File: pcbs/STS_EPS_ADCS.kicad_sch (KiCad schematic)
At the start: 25 parts, among them U10 MAX11632EEGT, U5 MAX11632EEGT, U6 MAX11632EEGT, U7 MAX11632EEGT, U8 MAX11632EEGT, U9 MAX11632EEGT

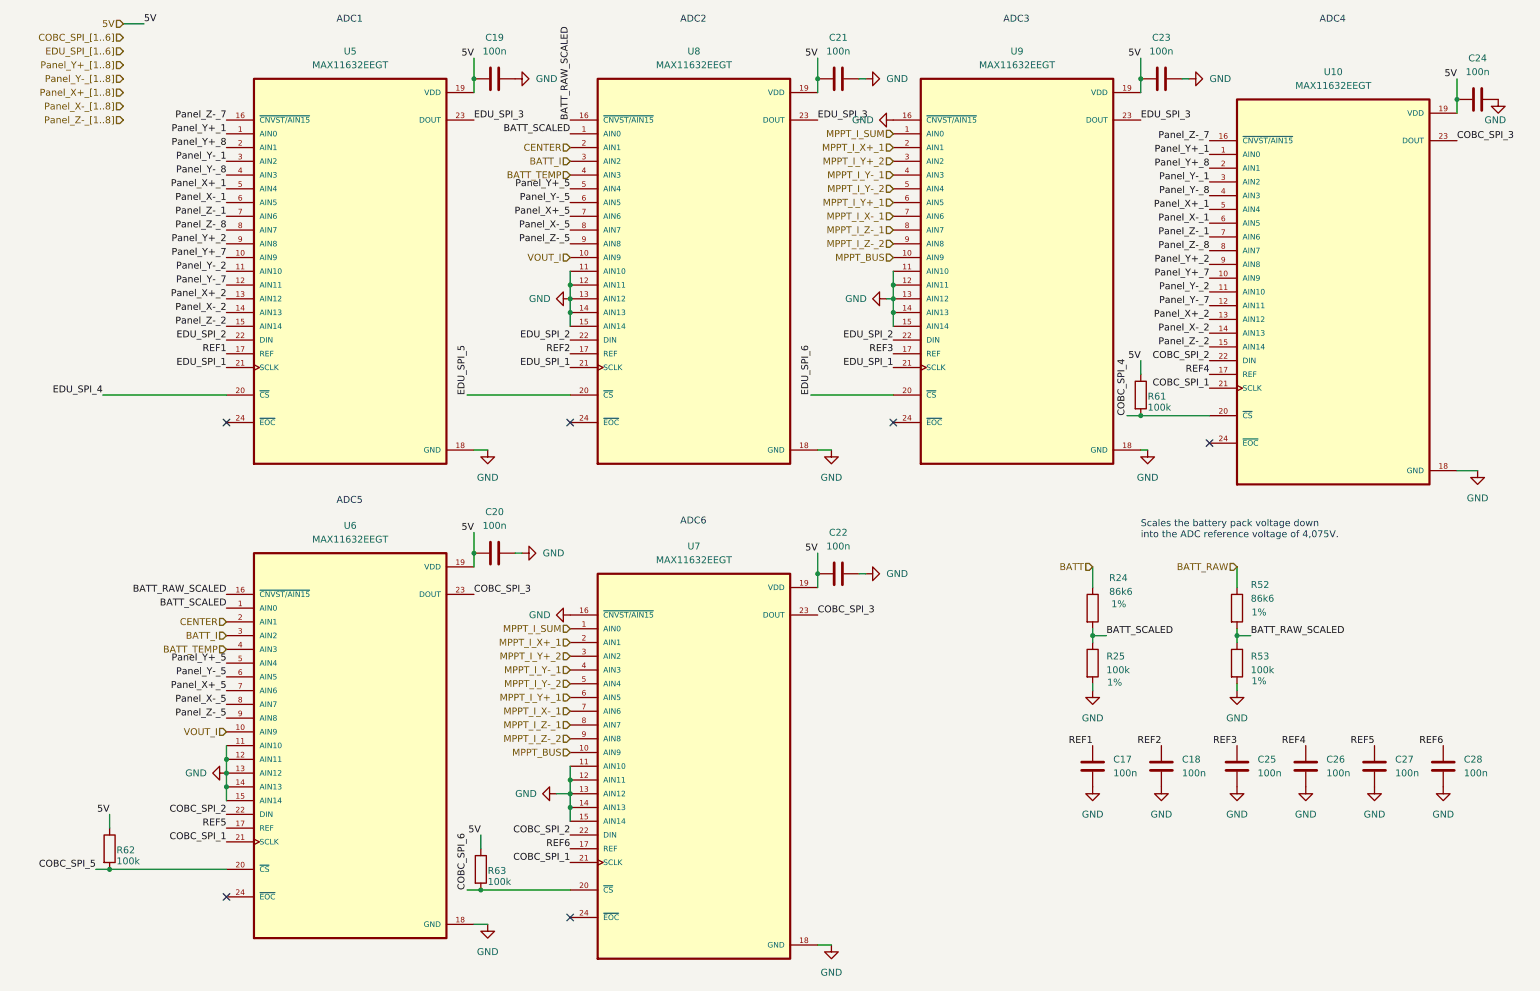
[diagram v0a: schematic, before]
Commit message: Changed net labels of the panel connectors, so they are consistent with the name of the respective connector.
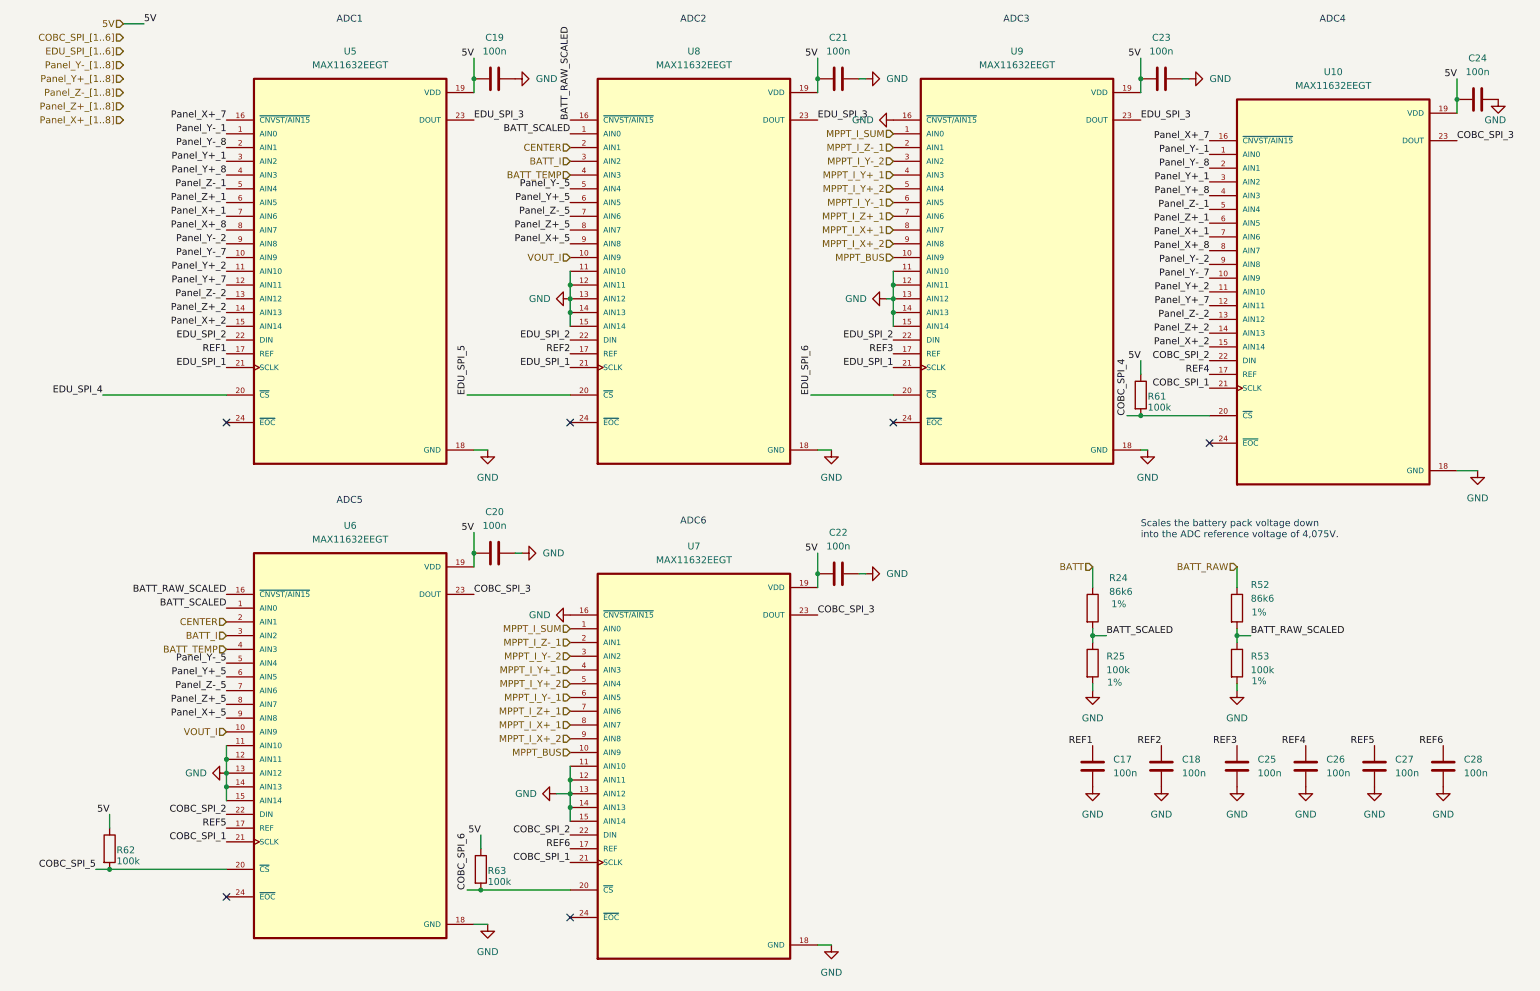
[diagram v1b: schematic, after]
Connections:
- net MPPT_I_X+_1: now also U7.8 (AIN7), U9.8 (AIN7); no longer U7.2 (AIN1), U9.2 (AIN1)
- net MPPT_I_Y+_1: now also U7.4 (AIN3), U9.4 (AIN3); no longer U7.6 (AIN5), U9.6 (AIN5)
- net MPPT_I_Y+_2: now also U7.5 (AIN4), U9.5 (AIN4); no longer U7.3 (AIN2), U9.3 (AIN2)
- net MPPT_I_Y-_1: now also U7.6 (AIN5), U9.6 (AIN5); no longer U7.4 (AIN3), U9.4 (AIN3)
- net MPPT_I_Y-_2: now also U7.3 (AIN2), U9.3 (AIN2); no longer U7.5 (AIN4), U9.5 (AIN4)
- net MPPT_I_Z-_1: now also U7.2 (AIN1), U9.2 (AIN1); no longer U7.8 (AIN7), U9.8 (AIN7)
- net Panel_X+_1: now also U10.7 (AIN6), U5.7 (AIN6); no longer U10.5 (AIN4), U5.5 (AIN4)
- net Panel_X+_2: now also U10.15 (AIN14), U5.15 (AIN14); no longer U10.13 (AIN12), U5.13 (AIN12)
- net Panel_X+_5: now also U6.9 (AIN8), U8.9 (AIN8); no longer U6.7 (AIN6), U8.7 (AIN6)
- net Panel_Y+_1: now also U10.3 (AIN2), U5.3 (AIN2); no longer U10.1 (AIN0), U5.1 (AIN0)
- net Panel_Y+_2: now also U10.11 (AIN10), U5.11 (AIN10); no longer U10.9 (AIN8), U5.9 (AIN8)
- net Panel_Y+_5: now also U6.6 (AIN5), U8.6 (AIN5); no longer U6.5 (AIN4), U8.5 (AIN4)
- net Panel_Y+_7: now also U10.12 (AIN11), U5.12 (AIN11); no longer U10.10 (AIN9), U5.10 (AIN9)
- net Panel_Y+_8: now also U10.4 (AIN3), U5.4 (AIN3); no longer U10.2 (AIN1), U5.2 (AIN1)
- net Panel_Y-_1: now also U10.1 (AIN0), U5.1 (AIN0); no longer U10.3 (AIN2), U5.3 (AIN2)
- net Panel_Y-_2: now also U10.9 (AIN8), U5.9 (AIN8); no longer U10.11 (AIN10), U5.11 (AIN10)
- net Panel_Y-_5: now also U6.5 (AIN4), U8.5 (AIN4); no longer U6.6 (AIN5), U8.6 (AIN5)
- net Panel_Y-_7: now also U10.10 (AIN9), U5.10 (AIN9); no longer U10.12 (AIN11), U5.12 (AIN11)
- net Panel_Y-_8: now also U10.2 (AIN1), U5.2 (AIN1); no longer U10.4 (AIN3), U5.4 (AIN3)
- net Panel_Z-_1: now also U10.5 (AIN4), U5.5 (AIN4); no longer U10.7 (AIN6), U5.7 (AIN6)
- net Panel_Z-_2: now also U10.13 (AIN12), U5.13 (AIN12); no longer U10.15 (AIN14), U5.15 (AIN14)
- net Panel_Z-_5: now also U6.7 (AIN6), U8.7 (AIN6); no longer U6.9 (AIN8), U8.9 (AIN8)
- net MPPT_I_X-_1 renamed MPPT_I_Z+_1
- net MPPT_I_Z-_2 renamed MPPT_I_X+_2
- net Panel_X-_1 renamed Panel_Z+_1
- net Panel_X-_2 renamed Panel_Z+_2
- net Panel_X-_5 renamed Panel_Z+_5
- net Panel_Z-_7 renamed Panel_X+_7
- net Panel_Z-_8 renamed Panel_X+_8

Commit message: Started adding part numbers to passive components.
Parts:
- C17, C18, C19, C20, C21, C22, C23, C24, C25, C26, C27, C28: Part Nr. (none) -> C0805T104K1RCLTU
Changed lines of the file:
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@@
 			)
 		)
+		(property "Part Nr." "C0805T104K1RCLTU"
+			(at 97.79 114.3 0)
+			(effects
+				(font
+					(size 1.27 1.27)
+				)
+				(hide yes)
+			)
+		)
 		(pin "1"
 		)
@@
 			)
 		)
+		(property "Part Nr." "C0805T104K1RCLTU"
+			(at 273.05 153.67 0)
+			(effects
+				(font
+					(size 1.27 1.27)
+				)
+				(hide yes)
+			)
+		)
 		(pin "1"
 		)
@@
 			)
 		)
+		(property "Part Nr." "C0805T104K1RCLTU"
+			(at 161.29 26.67 0)
+			(effects
+				(font
+					(size 1.27 1.27)
+				)
+				(hide yes)
+			)
+		)
 		(pin "1"
 		)
@@
 			)
 		)
+		(property "Part Nr." "C0805T104K1RCLTU"
+			(at 220.98 153.67 0)
+			(effects
+				(font
+					(size 1.27 1.27)
+				)
+				(hide yes)
+			)
+		)
 		(pin "1"
 		)
@@
 			)
 		)
+		(property "Part Nr." "C0805T104K1RCLTU"
+			(at 279.4 30.48 0)
+			(effects
+				(font
+					(size 1.27 1.27)
+				)
+				(hide yes)
+			)
+		)
 		(pin "1"
 		)
@@
 			)
 		)
+		(property "Part Nr." "C0805T104K1RCLTU"
+			(at 97.79 26.67 0)
+			(effects
+				(font
+					(size 1.27 1.27)
+				)
+				(hide yes)
+			)
+		)
 		(pin "1"
 		)
@@
 			)
 		)
+		(property "Part Nr." "C0805T104K1RCLTU"
+			(at 208.28 153.67 0)
+			(effects
+				(font
+					(size 1.27 1.27)
+				)
+				(hide yes)
+			)
+		)
 		(pin "1"
 		)
@@
 			)
 		)
+		(property "Part Nr." "C0805T104K1RCLTU"
+			(at 161.29 118.11 0)
+			(effects
+				(font
+					(size 1.27 1.27)
+				)
+				(hide yes)
+			)
+		)
 		(pin "1"
 		)
@@
 			)
 		)
+		(property "Part Nr." "C0805T104K1RCLTU"
+			(at 260.35 153.67 0)
+			(effects
+				(font
+					(size 1.27 1.27)
+				)
+				(hide yes)
+			)
+		)
 		(pin "1"
 		)
@@
 			)
 		)
+		(property "Part Nr." "C0805T104K1RCLTU"
+			(at 234.95 153.67 0)
+			(effects
+				(font
+					(size 1.27 1.27)
+				)
+				(hide yes)
+			)
+		)
 		(pin "1"
 		)
@@
 			)
 		)
+		(property "Part Nr." "C0805T104K1RCLTU"
+			(at 247.65 153.67 0)
+			(effects
+				(font
+					(size 1.27 1.27)
+				)
+				(hide yes)
+			)
+		)
 		(pin "1"
 		)
@@
 			(at 220.98 26.67 0)
 			(effects
+				(font
+					(size 1.27 1.27)
+				)
+				(hide yes)
+			)
+		)
+		(property "Part Nr." "C0805T104K1RCLTU"
+			(at 220.98 26.67 0)
+			(effects

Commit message: Added part numbers to components of STS1_EPS_1.
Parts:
- R24, R52: Part Nr. (none) -> RCA080586K6FKEA
- R25, R53, R61, R62, R63: Part Nr. (none) -> TNPW0805100KFEEA
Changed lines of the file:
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@@
+			)
+		)
+		(property "Part Nr." "RCA080586K6FKEA"
+			(at 208.28 124.46 0)
+			(effects
+				(font
+					(size 1.27 1.27)
+				)
+				(hide yes)
 			)
 		)
@@
 			)
 		)
+		(property "Part Nr." "TNPW0805100KFEEA"
+			(at 234.95 134.62 0)
+			(effects
+				(font
+					(size 1.27 1.27)
+				)
+				(hide yes)
+			)
+		)
 		(pin "1"
 		)
@@
 			)
 		)
+		(property "Part Nr." "TNPW0805100KFEEA"
+			(at 26.67 168.91 0)
+			(effects
+				(font
+					(size 1.27 1.27)
+				)
+				(hide yes)
+			)
+		)
 		(pin "1"
 		)
@@
 			)
 		)
+		(property "Part Nr." "TNPW0805100KFEEA"
+			(at 217.17 85.09 0)
+			(effects
+				(font
+					(size 1.27 1.27)
+				)
+				(hide yes)
+			)
+		)
 		(pin "1"
 		)
@@
 			)
 		)
+		(property "Part Nr." "TNPW0805100KFEEA"
+			(at 208.28 134.62 0)
+			(effects
+				(font
+					(size 1.27 1.27)
+				)
+				(hide yes)
+			)
+		)
 		(pin "1"
 		)
@@
 			)
 		)
+		(property "Part Nr." "TNPW0805100KFEEA"
+			(at 95.25 172.72 0)
+			(effects
+				(font
+					(size 1.27 1.27)
+				)
+				(hide yes)
+			)
+		)
 		(pin "1"
 		)
@@
 			)
 		)
+		(property "Part Nr." "RCA080586K6FKEA"
+			(at 234.95 124.46 0)
+			(effects
+				(font
+					(size 1.27 1.27)
+				)
+				(hide yes)
+			)
+		)

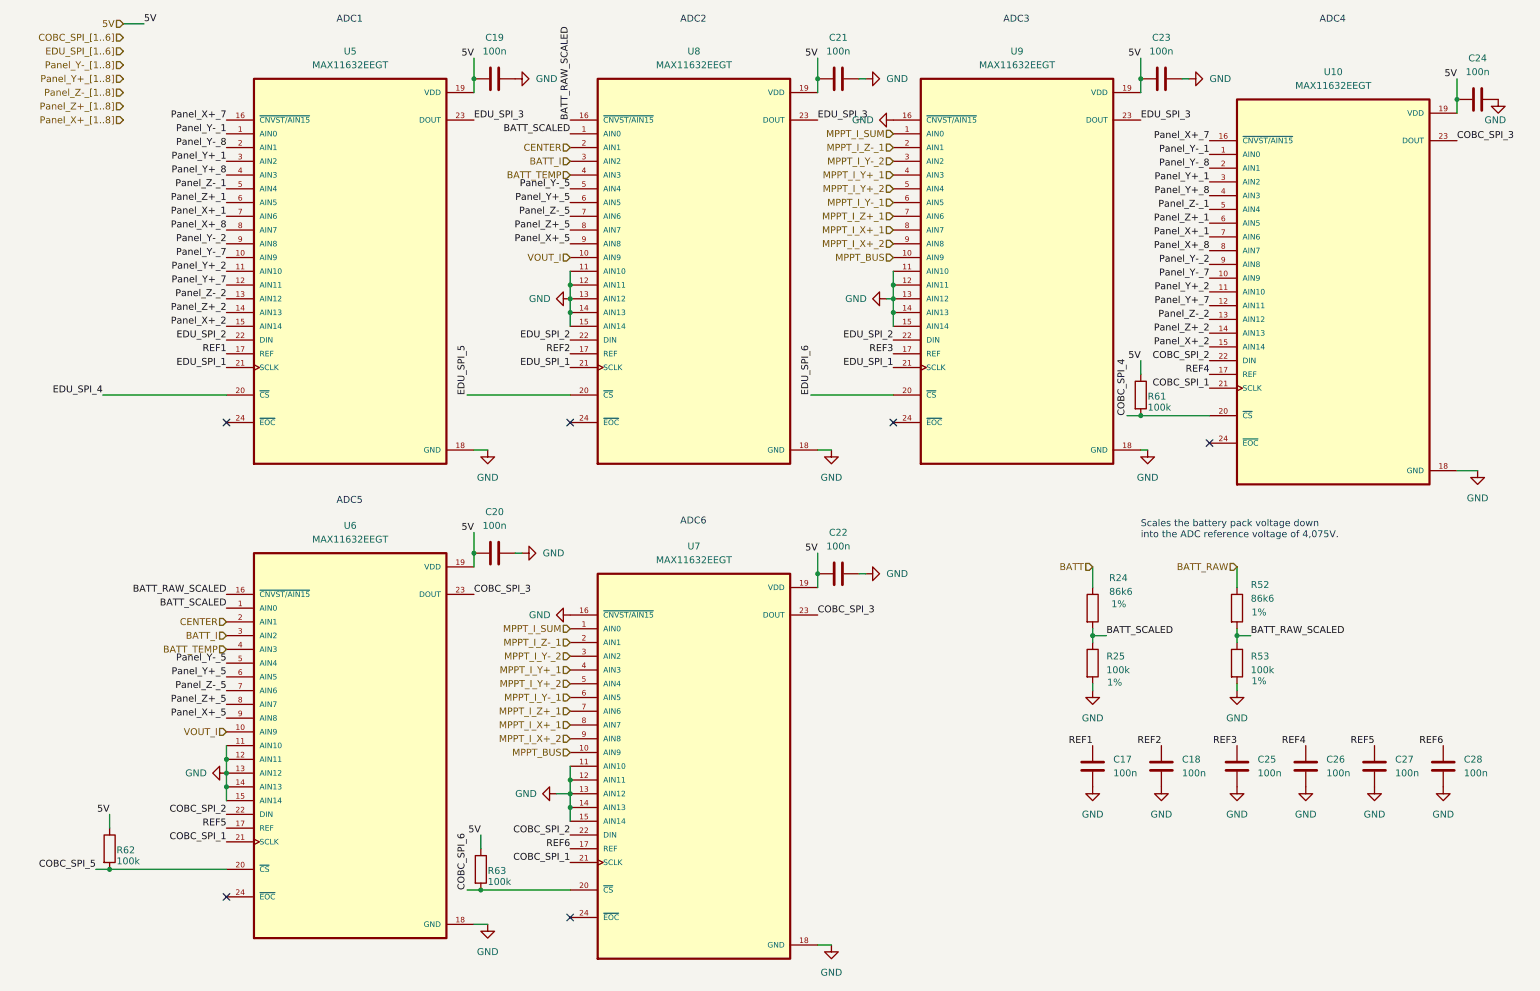
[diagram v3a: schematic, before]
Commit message: Added FETs to the CS pins of the EDU's housekeeping data interface.
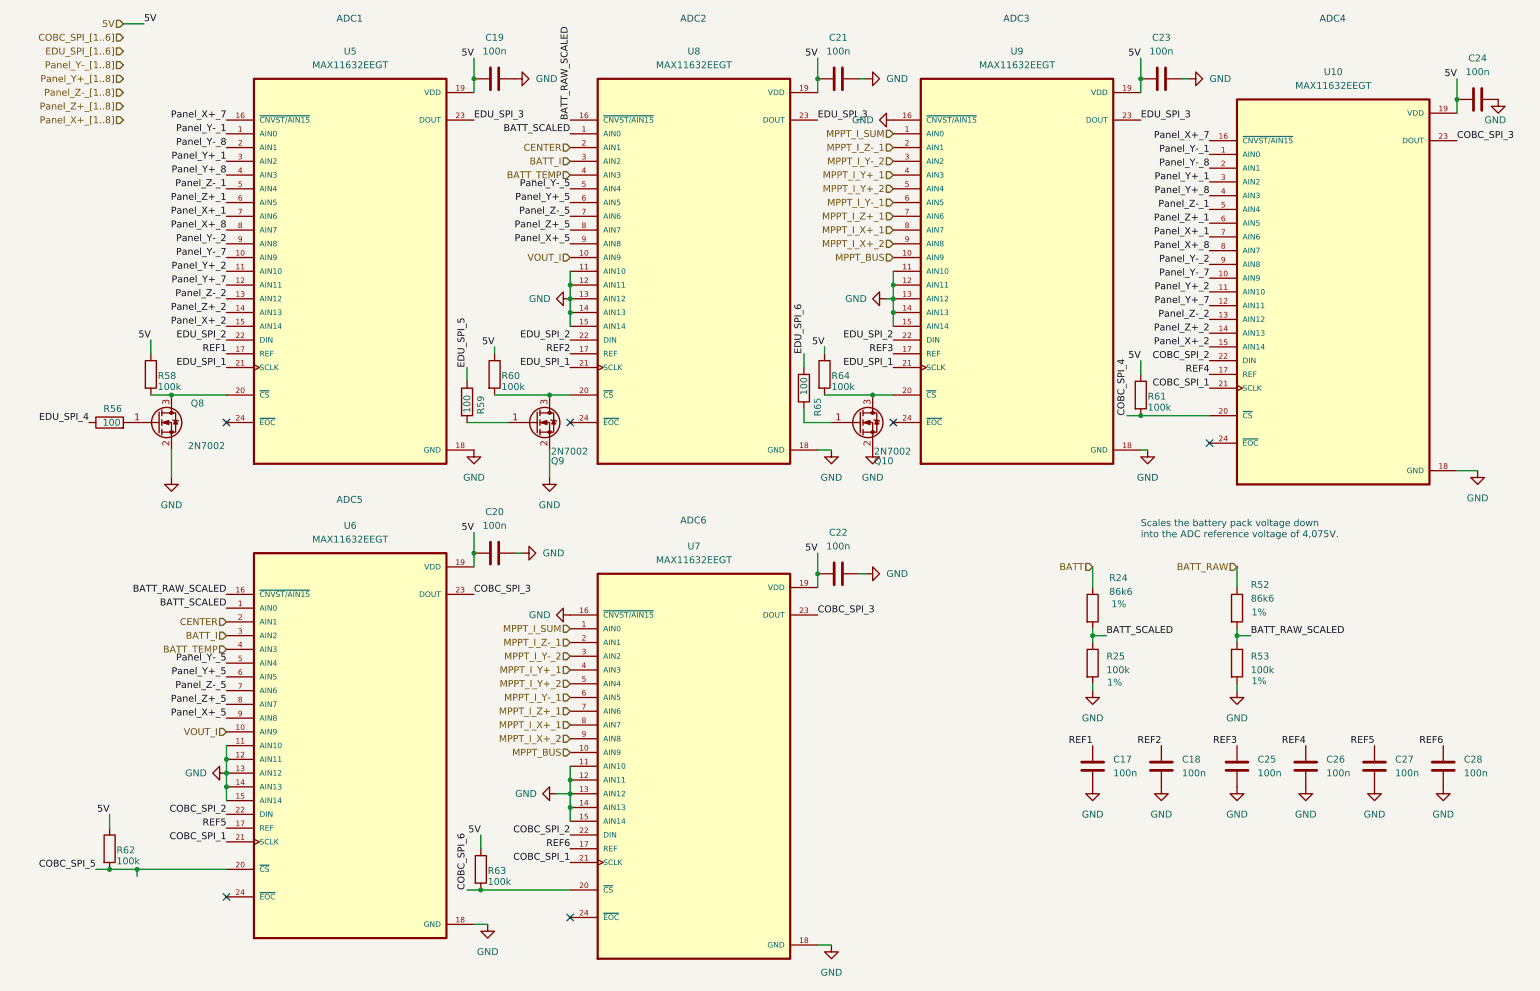
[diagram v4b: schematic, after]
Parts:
- added Q10, Q8, Q9: 2N7002, Package_TO_SOT_SMD:SOT-23, symbol Transistor_FET:2N7002
- added R56, R59, R65: 100, Resistor_SMD:R_0805_2012Metric, symbol Device:R
- added R58, R60, R64: 100k, Resistor_SMD:R_0805_2012Metric, symbol Device:R
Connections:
- net 5V: now also R58.1, R60.1, R64.1
- net EDU_SPI_4: now also R56.1; no longer U5.20 (~{CS})
- net EDU_SPI_5: now also R59.1; no longer U8.20 (~{CS})
- net EDU_SPI_6: now also R65.2; no longer U9.20 (~{CS})
- net GND: now also Q10.2 (S), Q8.2 (S), Q9.2 (S)
- new net: Q8.3 (D), R58.2, U5.20 (~{CS})
- new net: Q10.3 (D), R64.2, U9.20 (~{CS})
- new net: Q9.3 (D), R60.2, U8.20 (~{CS})
- new net: Q8.1 (G), R56.2
- new net: Q10.1 (G), R65.1
- new net: Q9.1 (G), R59.2

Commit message: Updated a few inconsistent part numbers.
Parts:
- R56, R59, R65: Part Nr. TNPW0805100KFEEA -> TNPW0805100RFETA
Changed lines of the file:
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@@
 			)
 		)
-		(property "Part Nr." "TNPW0805100KFEEA"
+		(property "Part Nr." "TNPW0805100RFETA"
 			(at 26.67 90.17 0)
 			(effects
@@
 			)
 		)
-		(property "Part Nr." "TNPW0805100KFEEA"
+		(property "Part Nr." "TNPW0805100RFETA"
 			(at 154.94 83.82 0)
 			(effects
@@
 			)
 		)
-		(property "Part Nr." "TNPW0805100KFEEA"
+		(property "Part Nr." "TNPW0805100RFETA"
 			(at 92.71 86.36 0)
 			(effects
